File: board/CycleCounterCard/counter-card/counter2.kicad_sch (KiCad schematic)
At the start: 19 parts, among them J1 Bus_Hydra_8bit, J2 74F86, J3 74F86, J4 74F86, J5 74F86, U1 74F191, U13 74F573, U2 74F573, U21 74F573, U22 74F191, U24 74F02, U27 74F00, U4 74F191, U6 74F573, U7 74F191

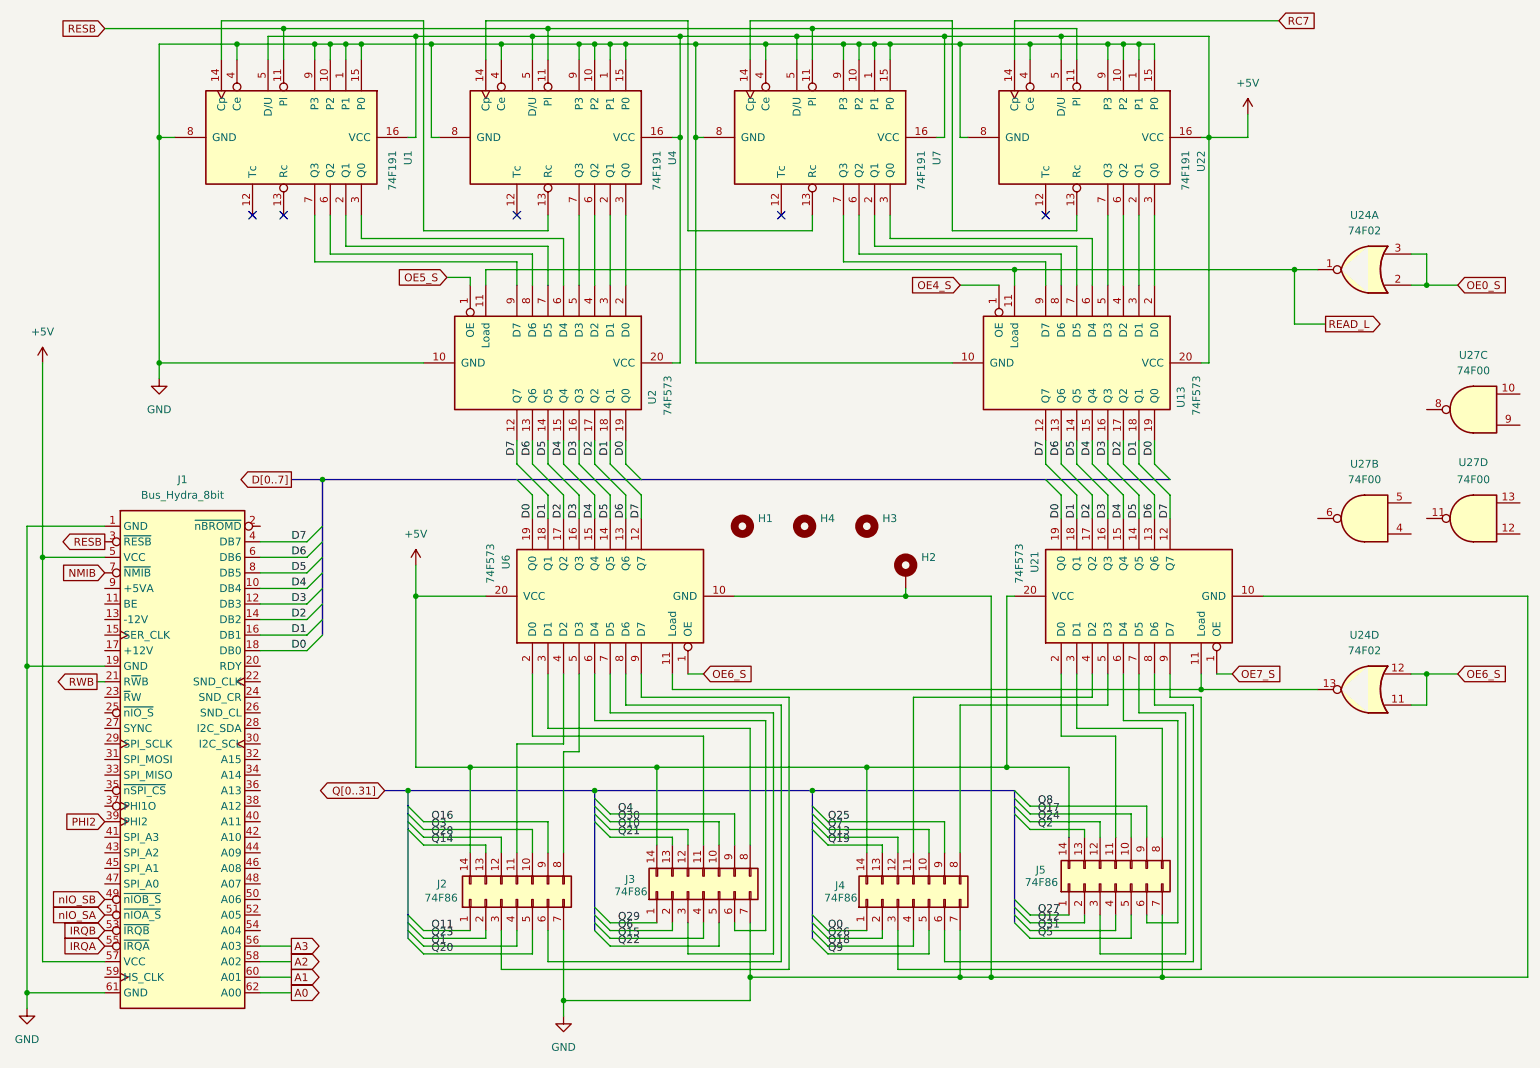
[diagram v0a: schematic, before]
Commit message: V2.0: wait states, GAL glue logic, serial clock and review fixes
Main board schematic:
- Replace the T4-T7 clock divider with RDY wait states. Fixed 7.16 MHz
  CPU clock; J36 selects 3.58 MHz for Rockwell parts. Waits are set per
  region through the write-only register at $FFF5 (reset = 3 waits).
- Move address decode, strobes, the wait-state generator, the IRQ
  encoder/latch/vector mux, ROM bank gating and DMA sync into seven GALs
  (U81-U86 ATF22V10C, U87 ATF16V8C), removing 29 ICs. CUPL sources,
  JEDECs and notes are in board/PLDs/V2.
- 1.8432 MHz serial clock, soft-power latch, -5V regulator, bulk caps,
  pull-ups, audio coupling/decoupling, GNDA tie, read-only Z register
  and other design-review fixes.
- New WaitStates and Support sheets; project symbol library
  hydra16.kicad_sym with sym-lib-table.

PCB updated from the schematic. Includes pending changes to the counter,
bus breakout and memory daughter card projects.

Firmware:
- Remove S_REGISTER; T/U/V/W now at $FFF0-$FFF3 to match the hardware.
- Add math.s and sound.s (included by os_main.s).
- Rebuild the 65C02 ROM image.

Co-Authored-By: Claude Opus 5.5 <noreply@anthropic.com>
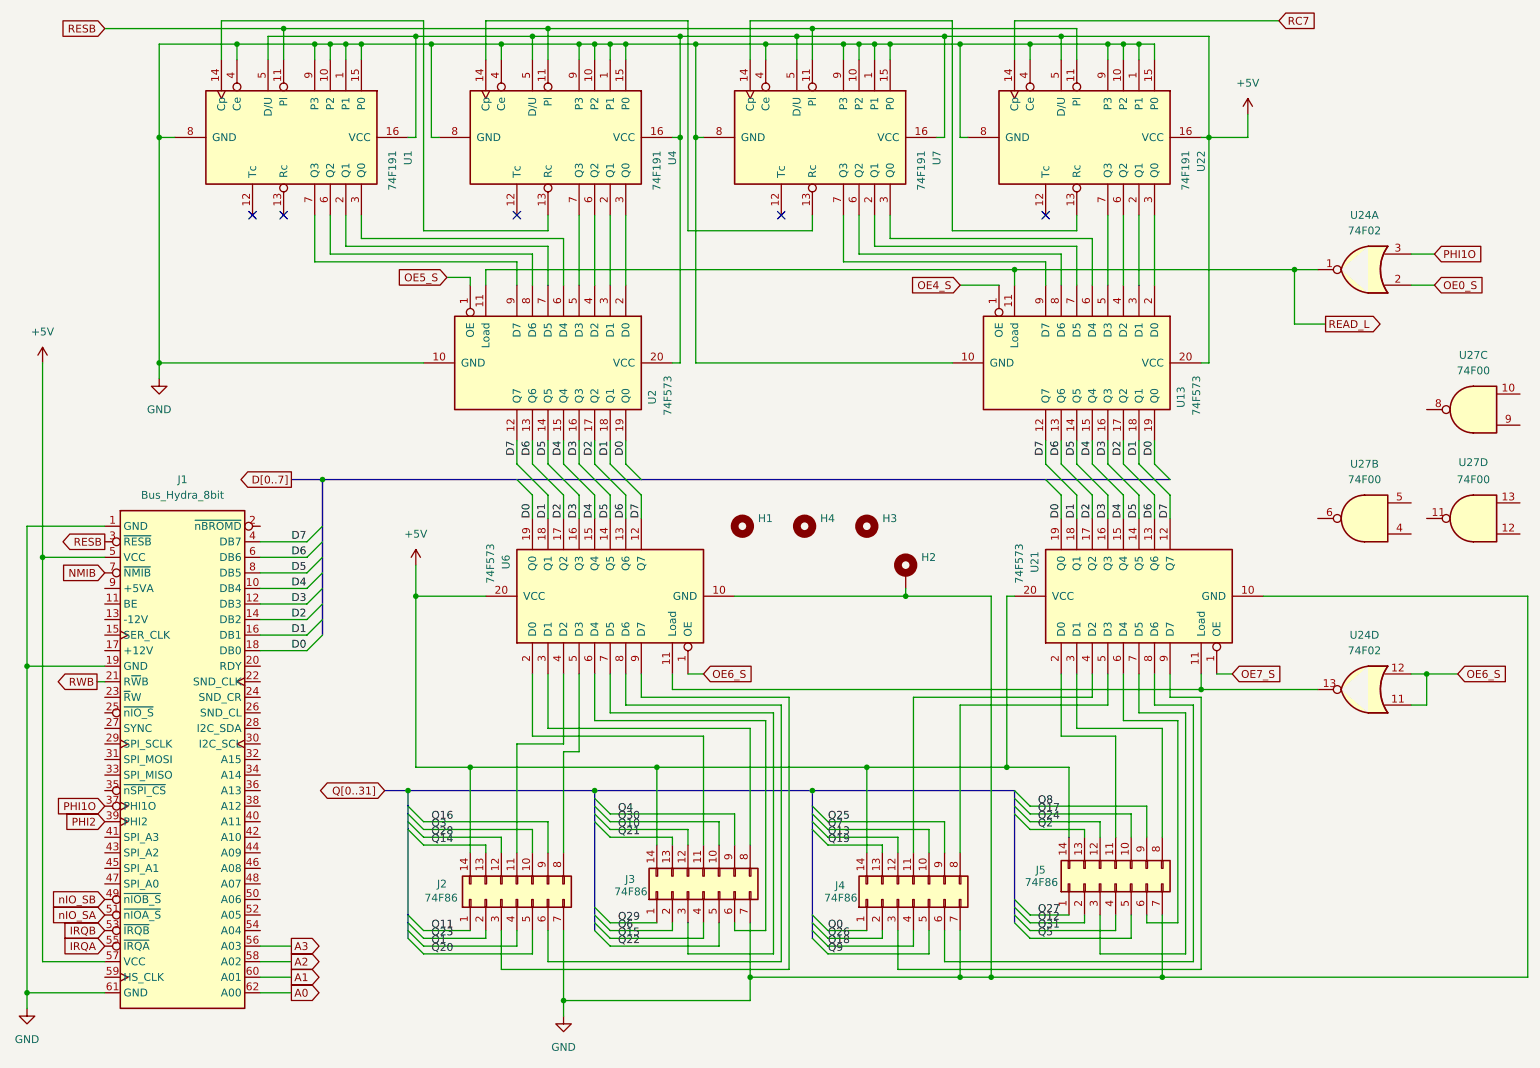
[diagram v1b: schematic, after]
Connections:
- net OE0_S: no longer U24.3
- net PHI1O: now reaches J1.37 (PHI1O)
- net PHI1O: now also U24.3
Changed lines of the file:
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@@
 	(title_block
 		(title "Clock Pulse Counter Card")
-		(rev "1.0")
+		(rev "1.2")
 	)
 	(junction
@@
 	)
 	(junction
-		(at 246.38 57.15)
-		(diameter 0)
-		(color 0 0 0 0)
-	)
-	(junction
 		(at 124.46 16.51)
 		(diameter 0)
@@
 	(wire
 		(pts
-			(xy 246.38 57.15) (xy 251.46 57.15)
+			(xy 243.84 57.15) (xy 247.65 57.15)
 		)
 		(stroke
@@
 	(wire
 		(pts
-			(xy 243.84 52.07) (xy 246.38 52.07)
+			(xy 243.84 52.07) (xy 247.65 52.07)
 		)
 		(stroke
@@
 	(wire
 		(pts
-			(xy 246.38 52.07) (xy 246.38 57.15)
-		)
-		(stroke
-			(width 0)
-			(type default)
-		)
-	)
-	(wire
-		(pts
 			(xy 157.48 149.86) (xy 157.48 148.59)
 		)
@@
 	(wire
 		(pts
-			(xy 243.84 57.15) (xy 246.38 57.15)
-		)
-		(stroke
-			(width 0)
-			(type default)
-		)
-	)
-	(wire
-		(pts
 			(xy 189.23 82.55) (xy 189.23 86.36)
 		)
@@
 		)
 	)
+	(global_label "PHI1O"
+		(shape input)
+		(at 30.48 142.24 180)
+		(fields_autoplaced yes)
+		(effects
+			(font
+				(size 1.27 1.27)
+			)
+			(justify right)
+		)
+		(property "Intersheetrefs" "${INTERSHEET_REFS}"
+			(at 21.7495 142.24 0)
+			(effects
+				(font
+					(size 1.27 1.27)
+				)
+				(justify right)
+				(hide yes)
+			)
+		)
+	)
 	(global_label "A2"
 		(shape output)
@@
 	(global_label "OE0_S"
 		(shape input)
-		(at 251.46 57.15 0)
+		(at 247.65 57.15 0)
 		(fields_autoplaced yes)
 		(effects
@@
 		)
 		(property "Intersheetrefs" "${INTERSHEET_REFS}"
-			(at 260.3113 57.15 0)
+			(at 256.5013 57.15 0)
 			(effects
 				(font
@@
 			(effects
 				(font
+					(size 1.27 1.27)
+				)
+				(justify right)
+				(hide yes)
+			)
+		)
+	)
+	(global_label "PHI1O"
+		(shape input)
+		(at 247.65 52.07 0)
+		(fields_autoplaced yes)
+		(effects
+			(font
+				(size 1.27 1.27)
+			)
+			(justify left)
+		)
+		(property "Intersheetrefs" "${INTERSHEET_REFS}"
+			(at 238.9195 52.07 0)
+			(effects
+				(font
